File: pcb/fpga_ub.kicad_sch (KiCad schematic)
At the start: 1 part

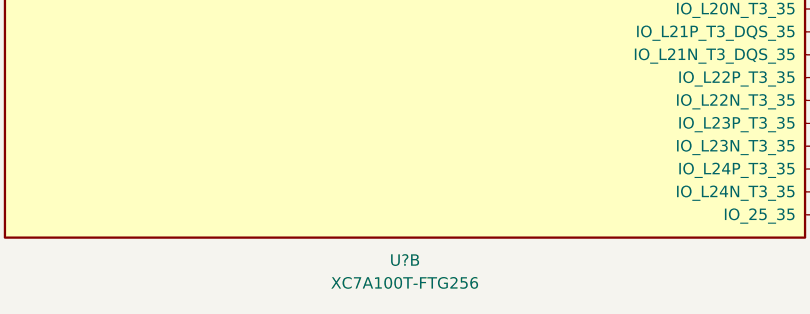
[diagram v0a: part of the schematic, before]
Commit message: add flash memory component for fpga
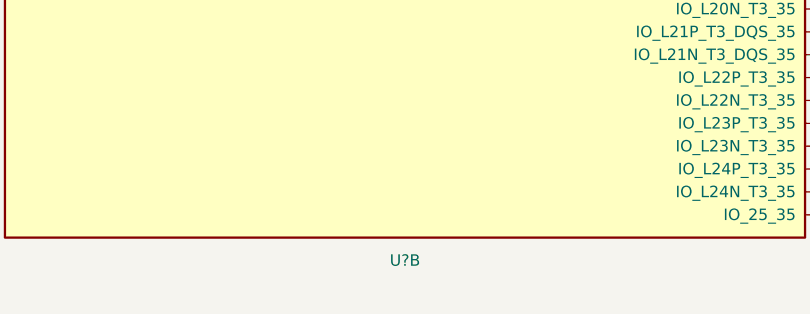
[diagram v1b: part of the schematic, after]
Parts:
- U?: value XC7A100T-FTG256 -> (none)
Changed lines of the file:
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@@
     (in_bom yes) (on_board yes) (fields_autoplaced)
     (property "Reference" "U?" (id 0) (at 93.98 179.07 0))
-    (property "Value" "XC7A100T-FTG256" (id 1) (at 93.98 181.61 0))
+    (property "Value" "" (id 1) (at 93.98 181.61 0))
     (property "Footprint" "" (id 2) (at 93.98 102.87 0)
       (effects (font (size 1.27 1.27)) hide)

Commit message: kicad said I needed to save
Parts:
- U?: value (none) -> XC7A100T-FTG256
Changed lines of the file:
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@@
     (in_bom yes) (on_board yes) (fields_autoplaced)
     (property "Reference" "U?" (id 0) (at 93.98 179.07 0))
-    (property "Value" "" (id 1) (at 93.98 181.61 0))
+    (property "Value" "XC7A100T-FTG256" (id 1) (at 93.98 181.61 0))
     (property "Footprint" "" (id 2) (at 93.98 102.87 0)
       (effects (font (size 1.27 1.27)) hide)
